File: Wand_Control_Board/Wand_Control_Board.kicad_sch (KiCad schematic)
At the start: 11 parts, among them J1 Conn_01x03_Socket, J2 Conn_01x03_Socket, J3 Conn_01x03_Socket, J4 Conn_01x03_Pin, J5 Conn_01x05_Socket, J8 Conn_01x02_Socket, J9 Conn_01x02_Pin, SW1 SW_SPDT_312, SW2 SW_SPDT_312, U1 ATtiny85-20P

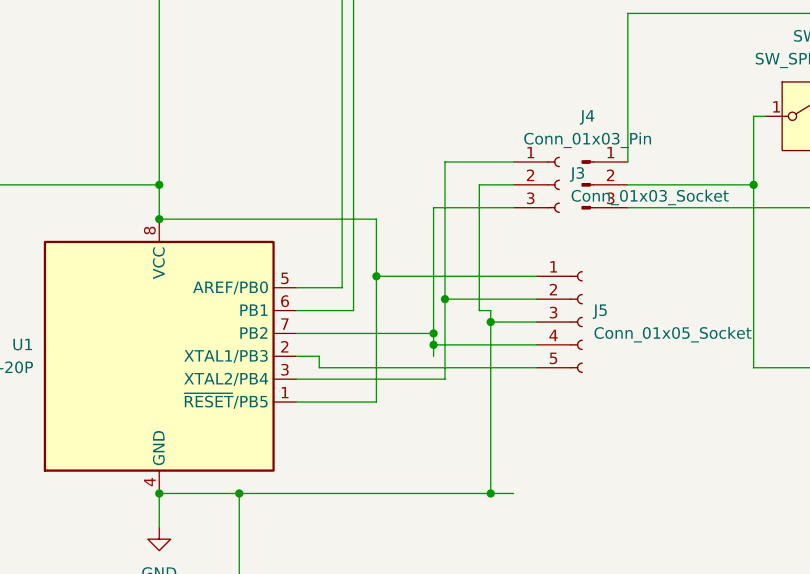
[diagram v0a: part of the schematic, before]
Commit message: added unneeded prog pad
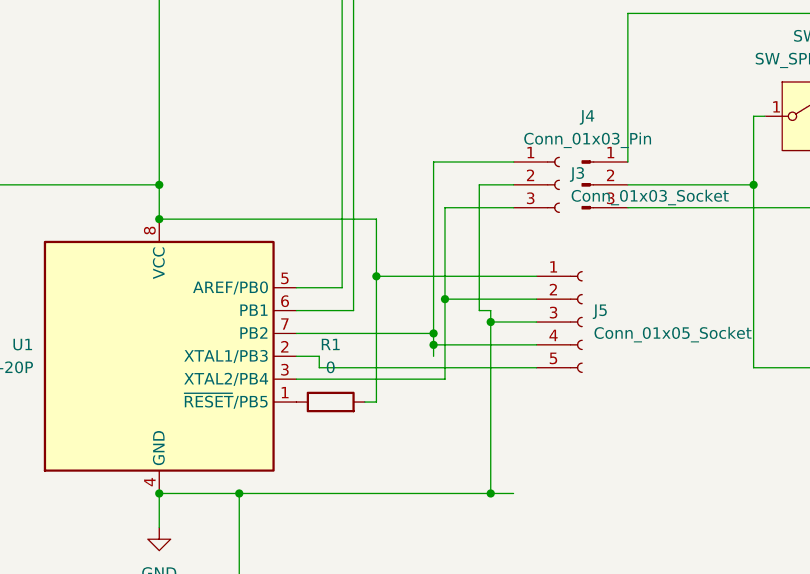
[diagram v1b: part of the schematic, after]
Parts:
- added R1: 0, Resistor_SMD:R_0805_2012Metric_Pad1.20x1.40mm_HandSolder, symbol Device:R
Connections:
- net VCC: now also R1.2; no longer U1.1 (~{RESET}/PB5)
- net at J5.2 (Pin_2), U1.3 (XTAL2/PB4): now also J3.3 (Pin_3); no longer J3.1 (Pin_1)
- net at J5.4 (Pin_4), U1.7 (PB2): now also J3.1 (Pin_1); no longer J3.3 (Pin_3)
- new net: R1.1, U1.1 (~{RESET}/PB5)
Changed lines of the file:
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@@
+	)
+	(junction
+		(at 135.89 91.44)
+		(diameter 0)
+		(color 0 0 0 0)
 	)
 	(junction
@@
 	)
 	(junction
-		(at 135.89 91.44)
-		(diameter 0)
-		(color 0 0 0 0)
-	)
-	(junction
 		(at 140.97 113.03)
 		(diameter 0)
@@
 	(wire
 		(pts
+			(xy 127 102.87) (xy 128.27 102.87)
+		)
+		(stroke
+			(width 0)
+			(type default)
+		)
+	)
+	(wire
+		(pts
 			(xy 78.74 104.14) (xy 78.74 134.62)
 		)
@@
 	(wire
 		(pts
-			(xy 135.89 76.2) (xy 135.89 91.44)
-		)
-		(stroke
-			(width 0)
-			(type default)
-		)
-	)
-	(wire
-		(pts
 			(xy 69.85 149.86) (xy 113.03 149.86)
 		)
@@
 	(wire
 		(pts
-			(xy 134.62 81.28) (xy 134.62 95.25)
-		)
-		(stroke
-			(width 0)
-			(type default)
-		)
-	)
-	(wire
-		(pts
-			(xy 143.51 81.28) (xy 134.62 81.28)
-		)
-		(stroke
-			(width 0)
-			(type default)
-		)
-	)
-	(wire
-		(pts
 			(xy 170.18 99.06) (xy 170.18 78.74)
 		)
@@
 	(wire
 		(pts
-			(xy 143.51 76.2) (xy 135.89 76.2)
-		)
-		(stroke
-			(width 0)
-			(type default)
-		)
-	)
-	(wire
-		(pts
 			(xy 78.74 88.9) (xy 78.74 104.14)
 		)
@@
 	(wire
 		(pts
+			(xy 134.62 76.2) (xy 143.51 76.2)
+		)
+		(stroke
+			(width 0)
+			(type default)
+		)
+	)
+	(wire
+		(pts
 			(xy 156.21 59.69) (xy 185.42 59.69)
 		)
@@
 	(wire
 		(pts
+			(xy 134.62 76.2) (xy 134.62 95.25)
+		)
+		(stroke
+			(width 0)
+			(type default)
+		)
+	)
+	(wire
+		(pts
 			(xy 64.77 88.9) (xy 78.74 88.9)
 		)
@@
 	(wire
 		(pts
+			(xy 135.89 81.28) (xy 135.89 91.44)
+		)
+		(stroke
+			(width 0)
+			(type default)
+		)
+	)
+	(wire
+		(pts
 			(xy 113.03 147.32) (xy 113.03 149.86)
 		)
@@
 	(wire
 		(pts
+			(xy 143.51 81.28) (xy 135.89 81.28)
+		)
+		(stroke
+			(width 0)
+			(type default)
+		)
+	)
+	(wire
+		(pts
 			(xy 134.62 95.25) (xy 134.62 96.52)
 		)
@@
 	(wire
 		(pts
-			(xy 128.27 102.87) (xy 119.38 102.87)
-		)
-		(stroke
-			(width 0)
-			(type default)
-		)
-	)
-	(wire
-		(pts
 			(xy 175.26 143.51) (xy 154.94 143.51)
 		)
@@
 		)
 	)
+	(symbol
+		(lib_id "Device:R")
+		(at 123.19 102.87 90)
+		(unit 1)
+		(exclude_from_sim no)
+		(in_bom yes)
+		(on_board yes)
+		(dnp no)
+		(fields_autoplaced yes)
+		(property "Reference" "R1"
+			(at 123.19 96.52 90)
+			(effects
+				(font
+					(size 1.27 1.27)
+				)
+			)
+		)
+		(property "Value" "0"
+			(at 123.19 99.06 90)
+			(effects
+				(font
+					(size 1.27 1.27)
+				)
+			)
+		)
+		(property "Footprint" "Resistor_SMD:R_0805_2012Metric_Pad1.20x1.40mm_HandSolder"
+			(at 123.19 104.648 90)
+			(effects
+				(font
+					(size 1.27 1.27)
+				)
+				(hide yes)
+			)
+		)
+		(property "Datasheet" "~"
+			(at 123.19 102.87 0)
+			(effects
+				(font
+					(size 1.27 1.27)
+				)
+				(hide yes)
+			)
+		)
+		(property "Description" "Resistor"
+			(at 123.19 102.87 0)
+			(effects
+				(font
+					(size 1.27 1.27)
+				)
+				(hide yes)
+			)
+		)
+		(pin "2"
+		)
+		(pin "1"
+		)
+		(instances
+			(project ""
+				(path "/9538e4ed-27e6-4c37-b989-9859dc0d49e8"
+					(reference "R1")
+					(unit 1)
+				)
+			)
+		)
+	)

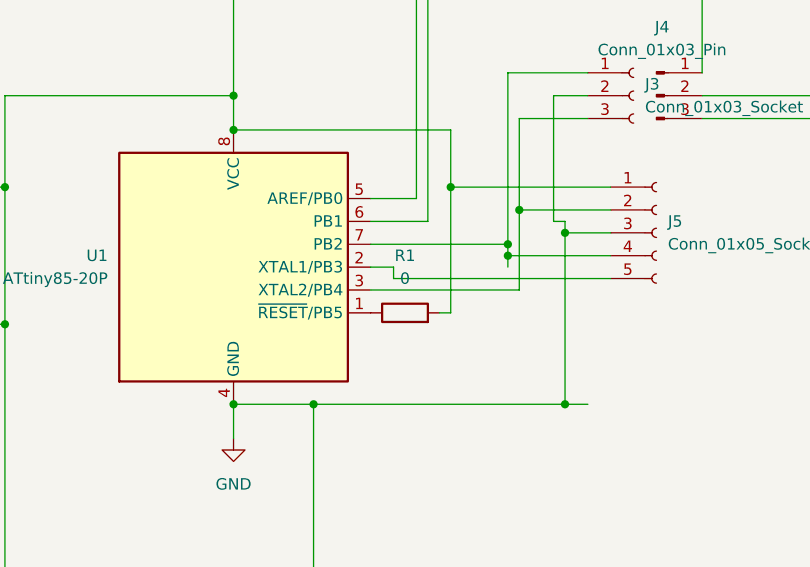
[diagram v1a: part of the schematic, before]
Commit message: removed unneeded progam pad
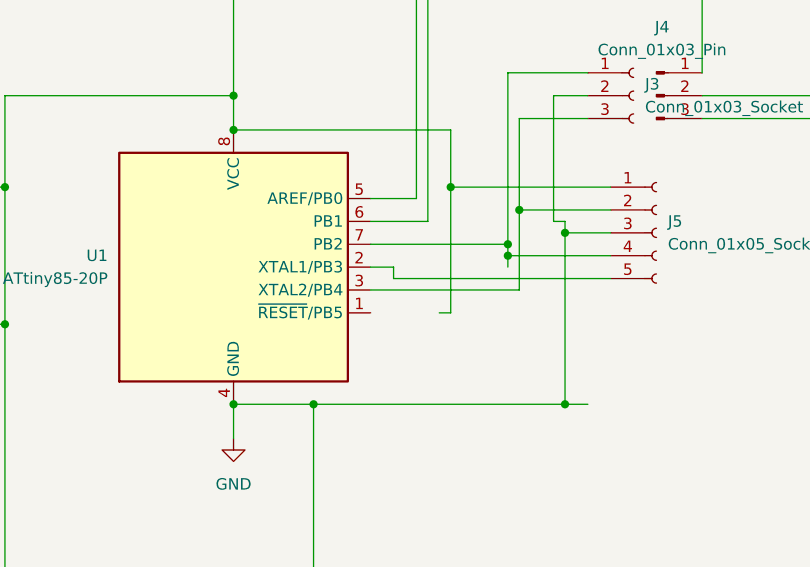
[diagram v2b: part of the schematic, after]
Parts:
- removed R1: 0, Resistor_SMD:R_0805_2012Metric_Pad1.20x1.40mm_HandSolder, symbol Device:R
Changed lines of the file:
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@@
-	)
-	(symbol
-		(lib_id "Device:R")
-		(at 123.19 102.87 90)
-		(unit 1)
-		(exclude_from_sim no)
-		(in_bom yes)
-		(on_board yes)
-		(dnp no)
-		(fields_autoplaced yes)
-		(property "Reference" "R1"
-			(at 123.19 96.52 90)
-			(effects
-				(font
-					(size 1.27 1.27)
-				)
-			)
-		)
-		(property "Value" "0"
-			(at 123.19 99.06 90)
-			(effects
-				(font
-					(size 1.27 1.27)
-				)
-			)
-		)
-		(property "Footprint" "Resistor_SMD:R_0805_2012Metric_Pad1.20x1.40mm_HandSolder"
-			(at 123.19 104.648 90)
-			(effects
-				(font
-					(size 1.27 1.27)
-				)
-				(hide yes)
-			)
-		)
-		(property "Datasheet" "~"
-			(at 123.19 102.87 0)
-			(effects
-				(font
-					(size 1.27 1.27)
-				)
-				(hide yes)
-			)
-		)
-		(property "Description" "Resistor"
-			(at 123.19 102.87 0)
-			(effects
-				(font
-					(size 1.27 1.27)
-				)
-				(hide yes)
-			)
-		)
-		(pin "2"
-		)
-		(pin "1"
-		)
-		(instances
-			(project ""
-				(path "/9538e4ed-27e6-4c37-b989-9859dc0d49e8"
-					(reference "R1")
-					(unit 1)
-				)
-			)
-		)
 	)
 	(symbol
